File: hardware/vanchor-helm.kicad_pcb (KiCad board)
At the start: 2 copper layers, 125 x 95 mm, 65 parts, among them J1 OPI_Z3_26PIN, J10 AUX 5V (screen), J11 AS5600, J12 PICO UTIL, J13 THRUST DRV, J14 BUCK 5V, J16 BATT 12V, J2 OPI_BREAKOUT, J22 SERVO MOTOR, J3 UART5 ttyAS5, J4 UART2 ttyAS2, J8 I2C3 spare, J9 FAN 5V, Q1 IRF9540N, U1 Pico 2, U7 BTN8982TA, U8 BTN8982TA

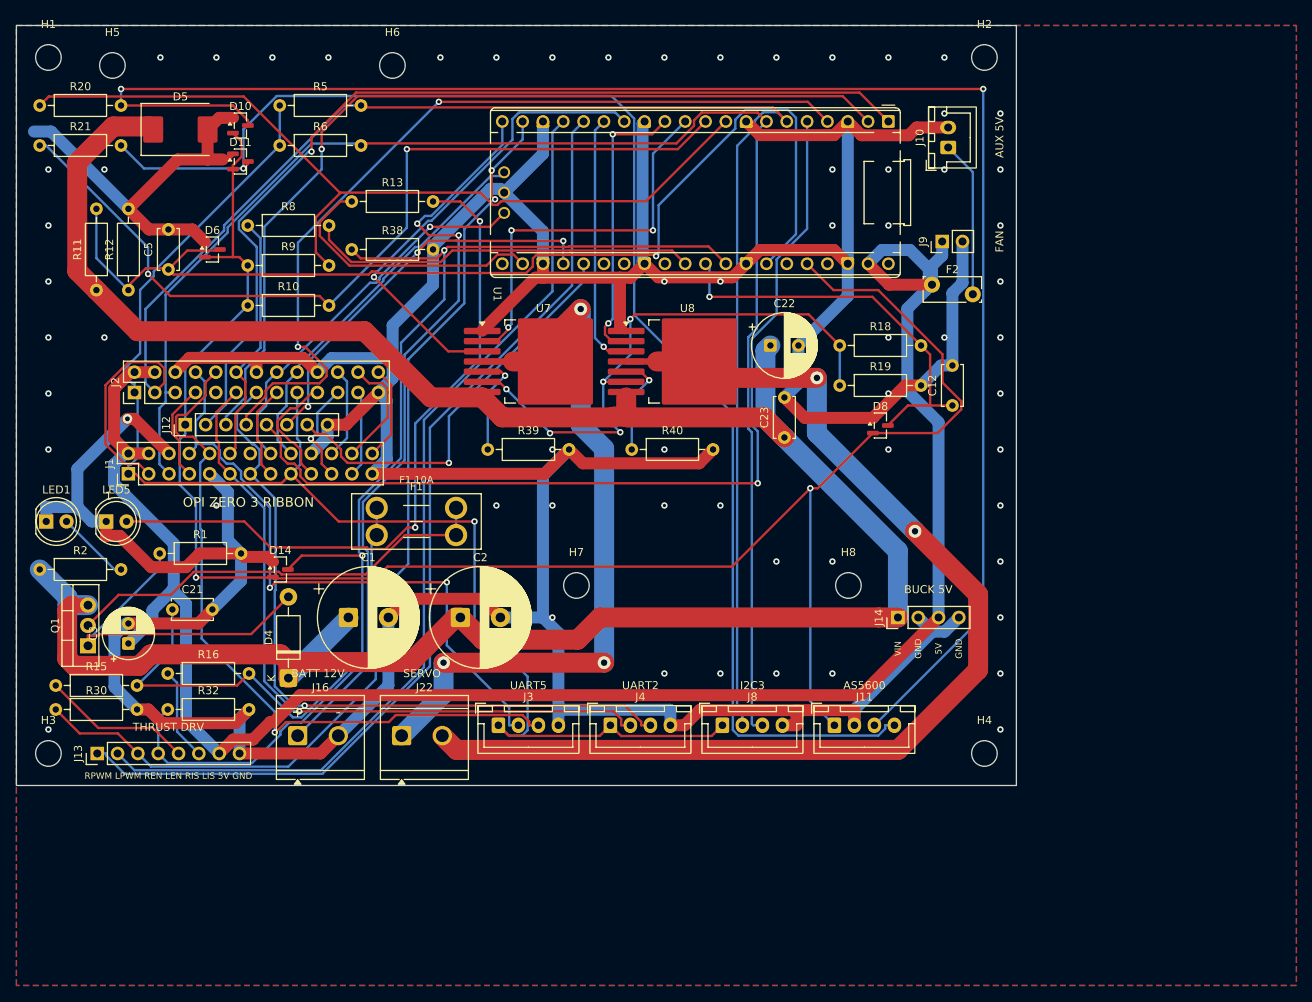
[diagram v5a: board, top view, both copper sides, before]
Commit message: wip: v4.2 XL4015 daughterboard (pre-lays, ENC parts near J11, tab straps) + thrust-driver spec & net-spec draft
Co-Authored-By: Claude Fable 5 <noreply@anthropic.com>
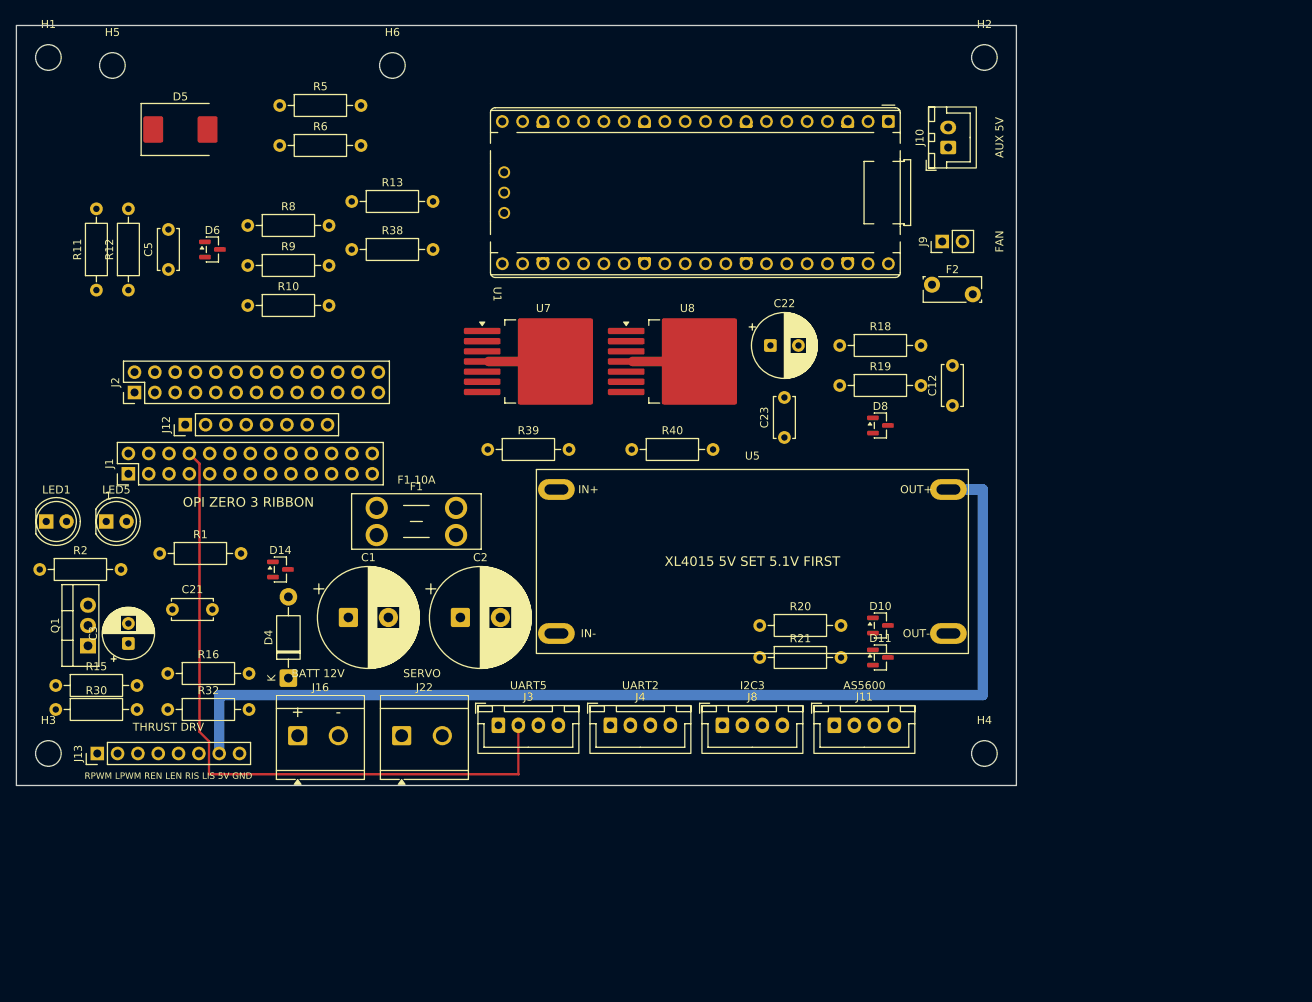
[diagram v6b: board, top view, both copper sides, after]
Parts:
- removed H7, H8: MountingHole_3.2mm_M3, MountingHole_3.2mm_M3
- removed J14: BUCK 5V, PinHeader_1x04_P2.54mm_Vertical
- added U5: XL4015 5A, XL4015_Module, F.Cu at (112.0, 87.0)
- moved R20 111.0 mm to (112.9, 95.0)
- moved R21 110.4 mm to (112.9, 99.0)
- moved D10 101.5 mm to (128.0, 95.0)
- moved D11 101.2 mm to (128.0, 99.0)
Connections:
- net /mcu/LED5_A renamed /control/LED5_A
- net /mcu/PICO_RUN renamed /control/PICO_RUN
- net /power/BATT_IN renamed /carrier/BATT_IN
- net /power/LED1_A renamed /carrier/LED1_A
- net /power/Q1_G renamed /carrier/Q1_G
- net /power/VIN_RAW renamed /carrier/VIN_RAW
- net /servo/ENC_SCL_J renamed /control/ENC_SCL_J
- net /servo/ENC_SDA_J renamed /control/ENC_SDA_J
- net /servo/SERVO_IS_RAW renamed /control/SERVO_IS_RAW
- net /servo/SR_A renamed /control/SR_A
- net /servo/SR_B renamed /control/SR_B
- net /thrust/L_IS renamed /control/L_IS
- net /thrust/R_IS renamed /control/R_IS
- J1 pad 14: (no net) -> unconnected-(J1-Pin_14-Pad14)
- J1 pad 20: GND -> unconnected-(J1-Pin_20-Pad20)
- J2 pad 9: (no net) -> unconnected-(J2-Pin_9-Pad9)
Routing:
- net GND: track 668.6 -> 0.00 mm, vias 62 -> 0
- net VIN: track 306.9 -> 0.00 mm
- net +3V3: track 230.4 -> 0.00 mm, vias 2 -> 0
- net /control/ENC_SDA_J: track 212.3 -> 0.00 mm, vias 2 -> 0
- net PI_SDA: track 211.2 -> 0.00 mm
- net PI_SCL: track 188.2 -> 0.00 mm
- net 3V3_PI: track 177.1 -> 0.00 mm, vias 1 -> 0
- net /control/ENC_SCL_J: track 177.0 -> 0.00 mm, vias 1 -> 0
- net THR_IS: track 159.7 -> 0.00 mm, vias 2 -> 0
- net VBAT_SENSE: track 138.4 -> 0.00 mm, vias 1 -> 0
- net SERVO_B: track 141.4 -> 5.00 mm, vias 2 -> 0
- net THR_R_EN: track 125.3 -> 0.00 mm, vias 2 -> 0
- net THR_RPWM: track 124.4 -> 0.00 mm
- net THR_LPWM: track 119.9 -> 0.00 mm
- net THR_L_EN: track 119.7 -> 0.00 mm, vias 2 -> 0
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- removed copper zone on B.Cu, net GND
- removed copper zone on F.Cu, net GND
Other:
- board text removed: "5V"
- board text removed: "BUCK 5V"
- board text removed: "GND"
- board text removed: "VIN"

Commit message: feat: v4.2 XL4015 buck daughterboard (U5 slotted pads, pre-laid 5V/UART5 spans, ENC parts at J11) — DRC clean
Co-Authored-By: Claude Fable 5 <noreply@anthropic.com>
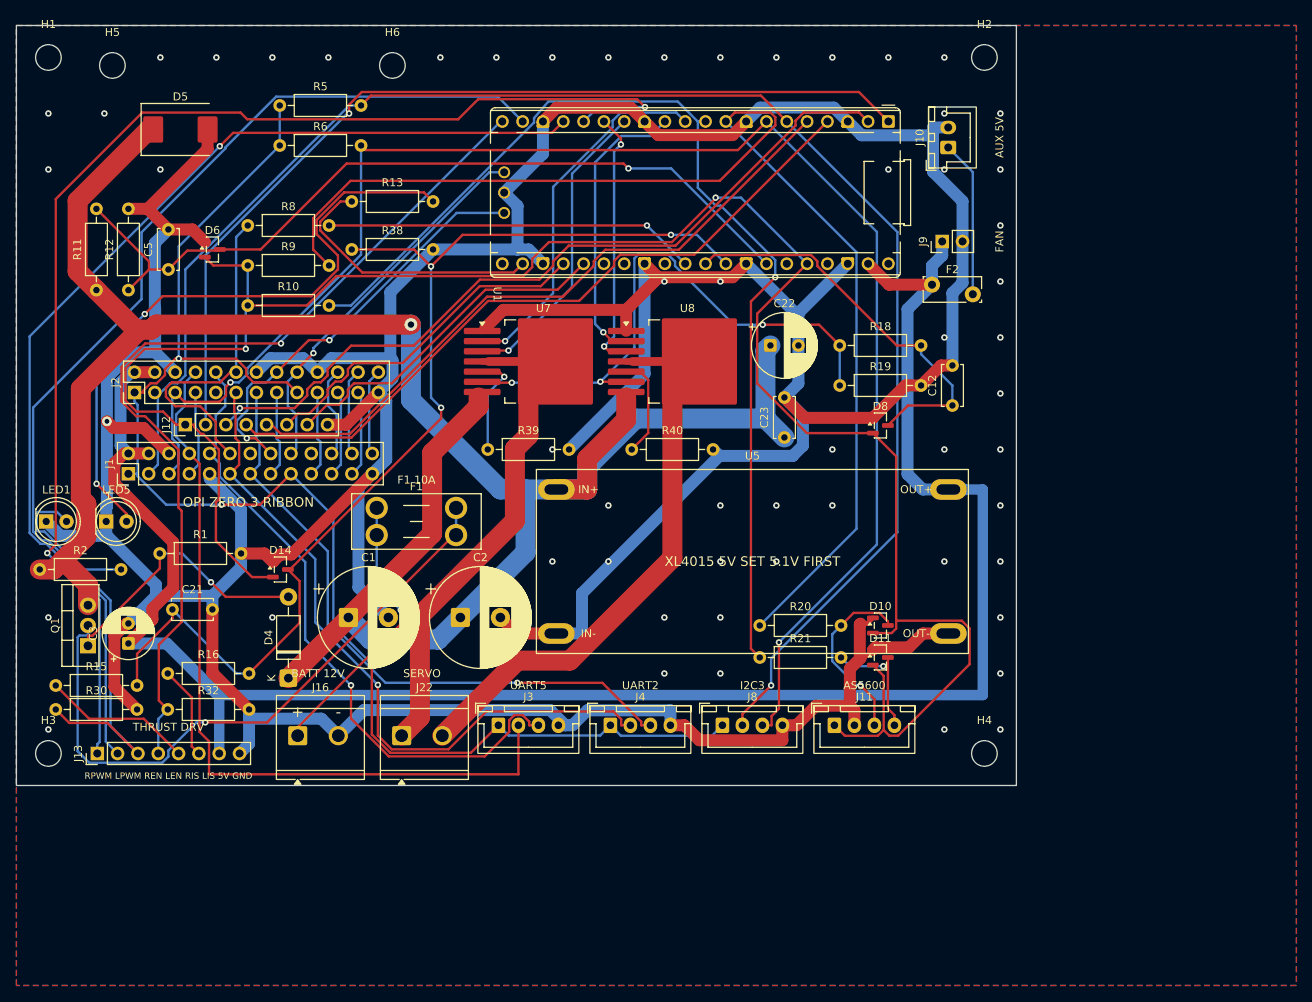
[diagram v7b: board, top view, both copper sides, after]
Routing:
- net GND: track 0.00 -> 680.2 mm, vias 0 -> 57
- net VIN: track 0.00 -> 286.4 mm, vias 0 -> 1
- net +3V3: track 0.00 -> 258.8 mm, vias 0 -> 2
- net PI_SDA: track 0.00 -> 203.3 mm, vias 0 -> 1
- net PI_SCL: track 0.00 -> 197.3 mm, vias 0 -> 2
- net 3V3_PI: track 0.00 -> 181.1 mm, vias 0 -> 3
- net THR_RPWM: track 0.00 -> 161.3 mm, vias 0 -> 2
- net ENC_SDA: track 0.00 -> 152.0 mm
- net THR_R_EN: track 0.00 -> 145.4 mm
- net THR_IS: track 0.00 -> 137.6 mm, vias 0 -> 3
- net THR_LPWM: track 0.00 -> 135.2 mm, vias 0 -> 1
- net ENC_SCL: track 0.00 -> 132.1 mm, vias 0 -> 1
- net PICO_GP0: track 0.00 -> 117.2 mm, vias 0 -> 1
- net THR_L_EN: track 0.00 -> 114.7 mm, vias 0 -> 1
- net +5V: track 130.8 -> 239.5 mm
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- added copper zone on B.Cu, net GND
- added copper zone on F.Cu, net GND
